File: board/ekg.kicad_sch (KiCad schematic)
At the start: 48 parts

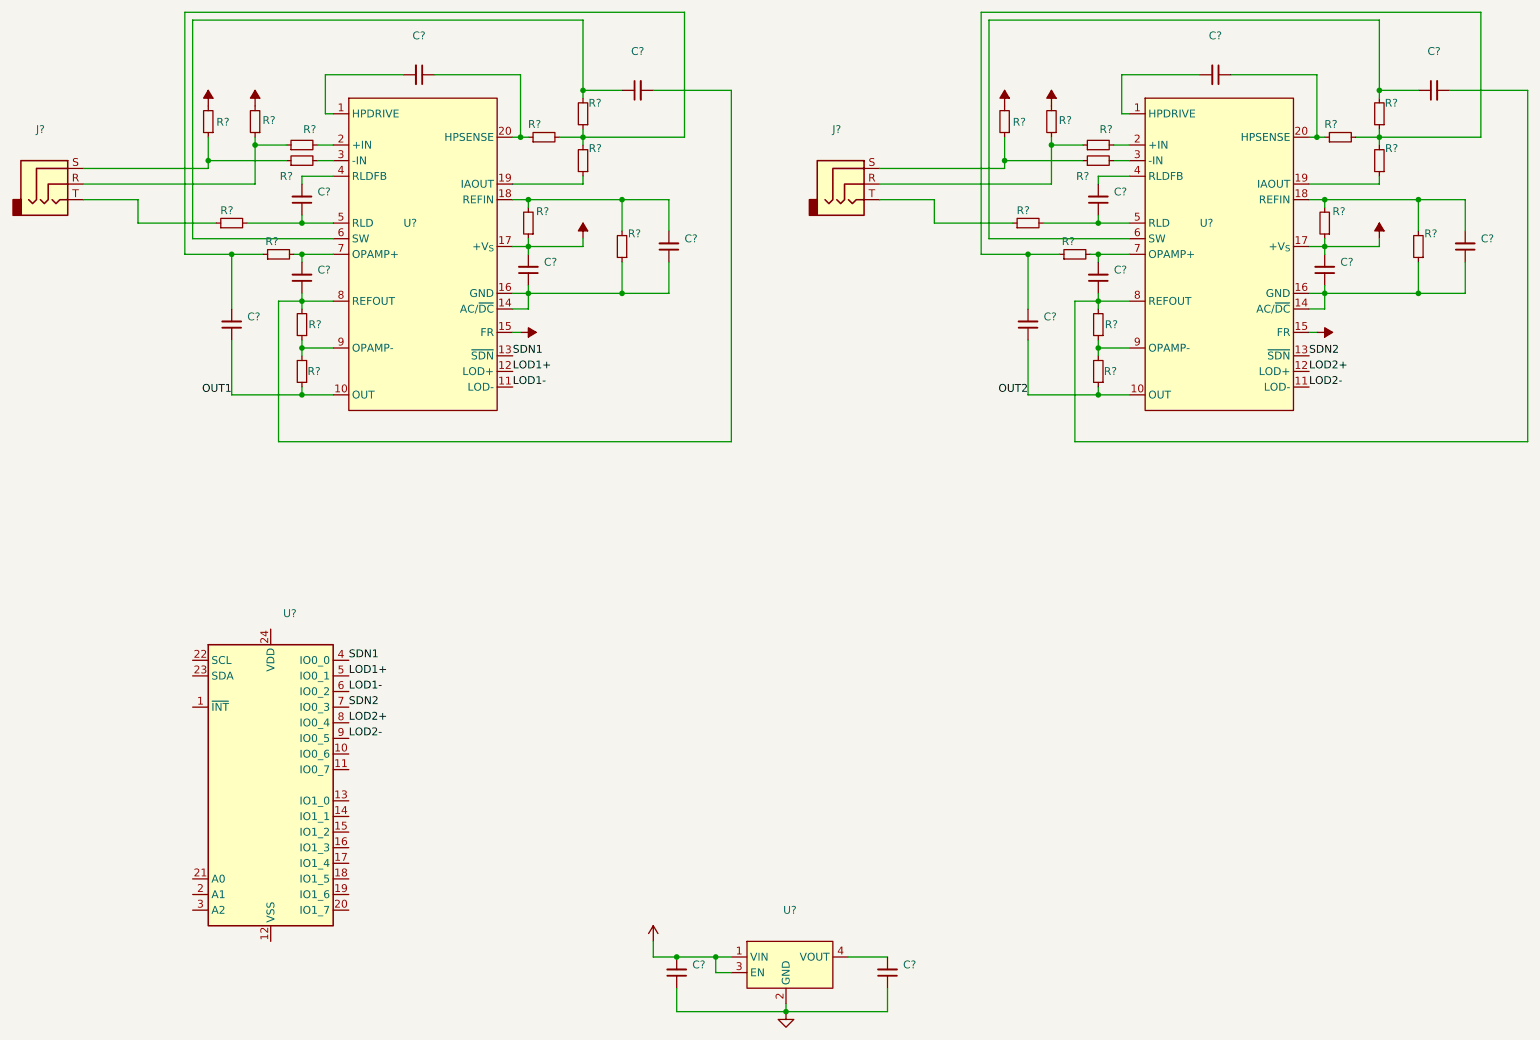
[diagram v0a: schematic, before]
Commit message: added ekg chip
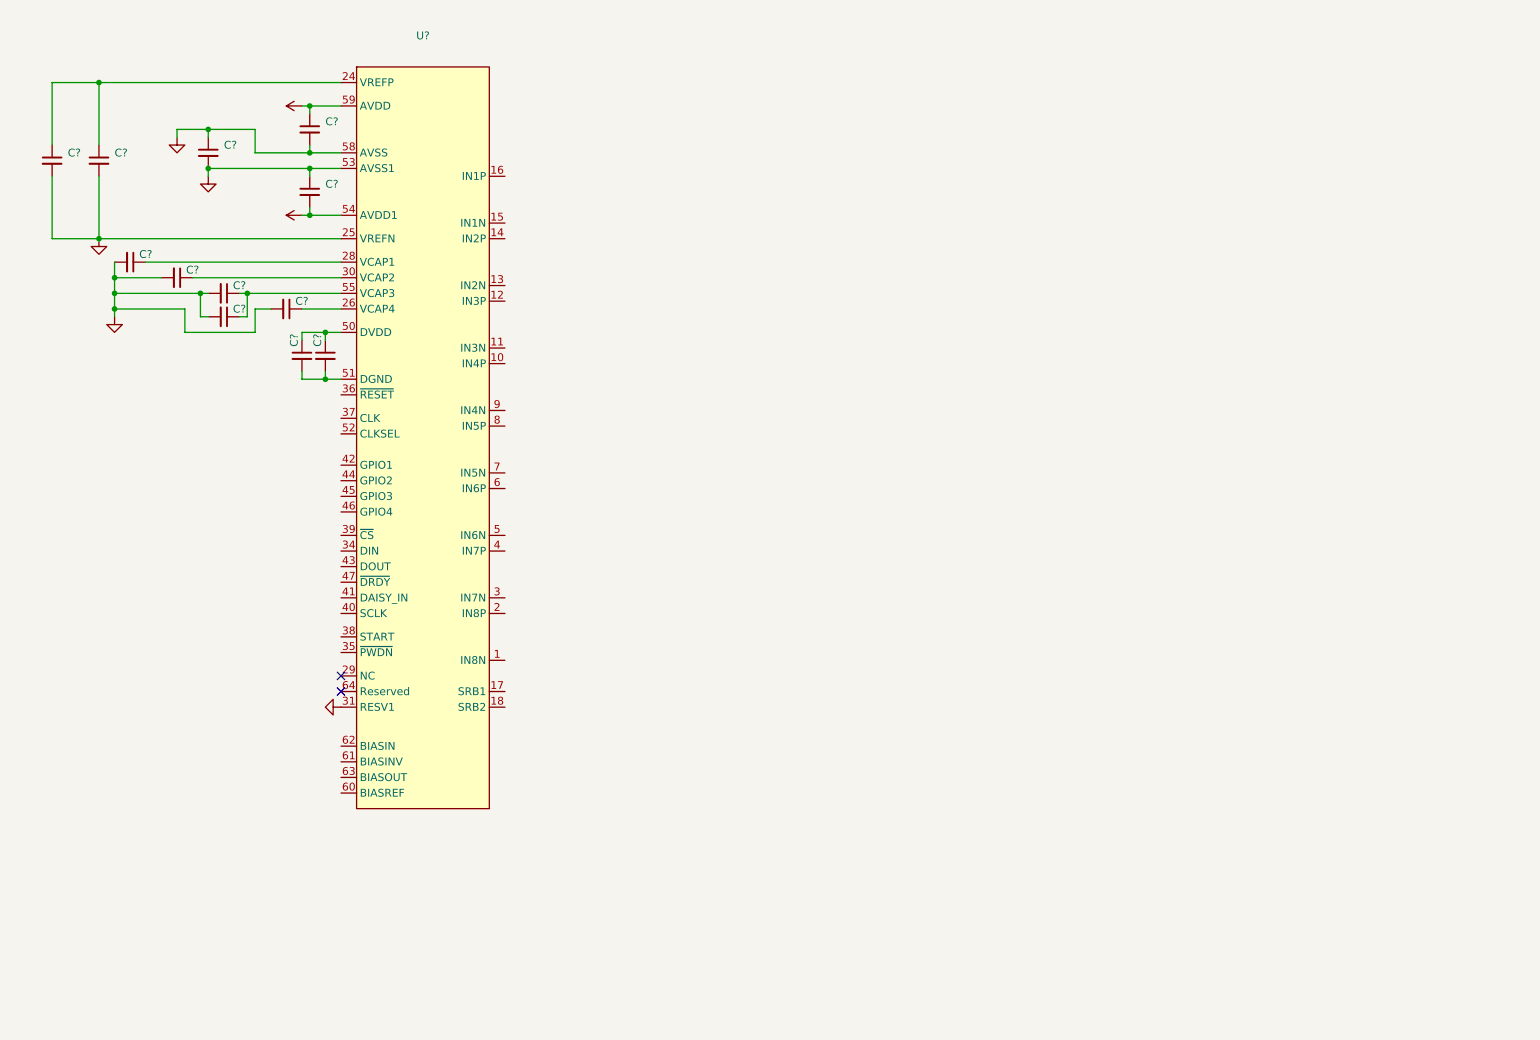
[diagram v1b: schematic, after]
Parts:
- removed C? (x9): (no value), symbol Device:C_Small
- removed C? (x7): ~, symbol Device:C_Small
- removed J? (x2): ~, symbol Connector:AudioJack3
- removed R? (x17): (no value), symbol Device:R_Small
- removed R? (x9): ~, symbol Device:R_Small
- removed U? (x2): ~, symbol ownLib:AD8232
- removed U?: (no value), symbol ownLib:ADP150
- removed U?: (no value), symbol Interface_Expansion:PCA9555D
- added C? (x11): (no value), symbol Device:C_Small
- added C?: ~, symbol Device:C_Small
- added U?: (no value), symbol ownLib:ADS1299-x
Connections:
- new net: C?.1, U?.26 (VCAP4)
- new net: C?.1, C?.1, U?.24 (VREFP)
- new net: U?.27 (NC), U?.29 (NC)
- new net: C?.1, U?.28 (VCAP1)
- new net: C?.1, U?.30 (VCAP2)
- new net: C?.1, C?.1, U?.55 (VCAP3)
- new net AVDD: C?.1, C?.2, U?.19 (AVDD), U?.21 (AVDD), U?.22 (AVDD), U?.54 (AVDD1), U?.56 (AVDD), U?.59 (AVDD)
- new net AVSS: C?.1, C?.1, C?.2, C?.2, C?.2, C?.2, C?.2, C?.2, C?.2, C?.2, C?.2, U?.20 (AVSS), U?.23 (AVSS), U?.25 (VREFN), U?.31 (RESV1), U?.32 (AVSS), U?.53 (AVSS1), U?.57 (AVSS), U?.58 (AVSS)
- new net DGND: C?.2, C?.2, U?.33 (DGND), U?.49 (DGND), U?.51 (DGND)
- new net DVDD: C?.1, C?.1, U?.48 (DVDD), U?.50 (DVDD)
- no-connect marks 0 -> 2

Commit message: added filter and imu
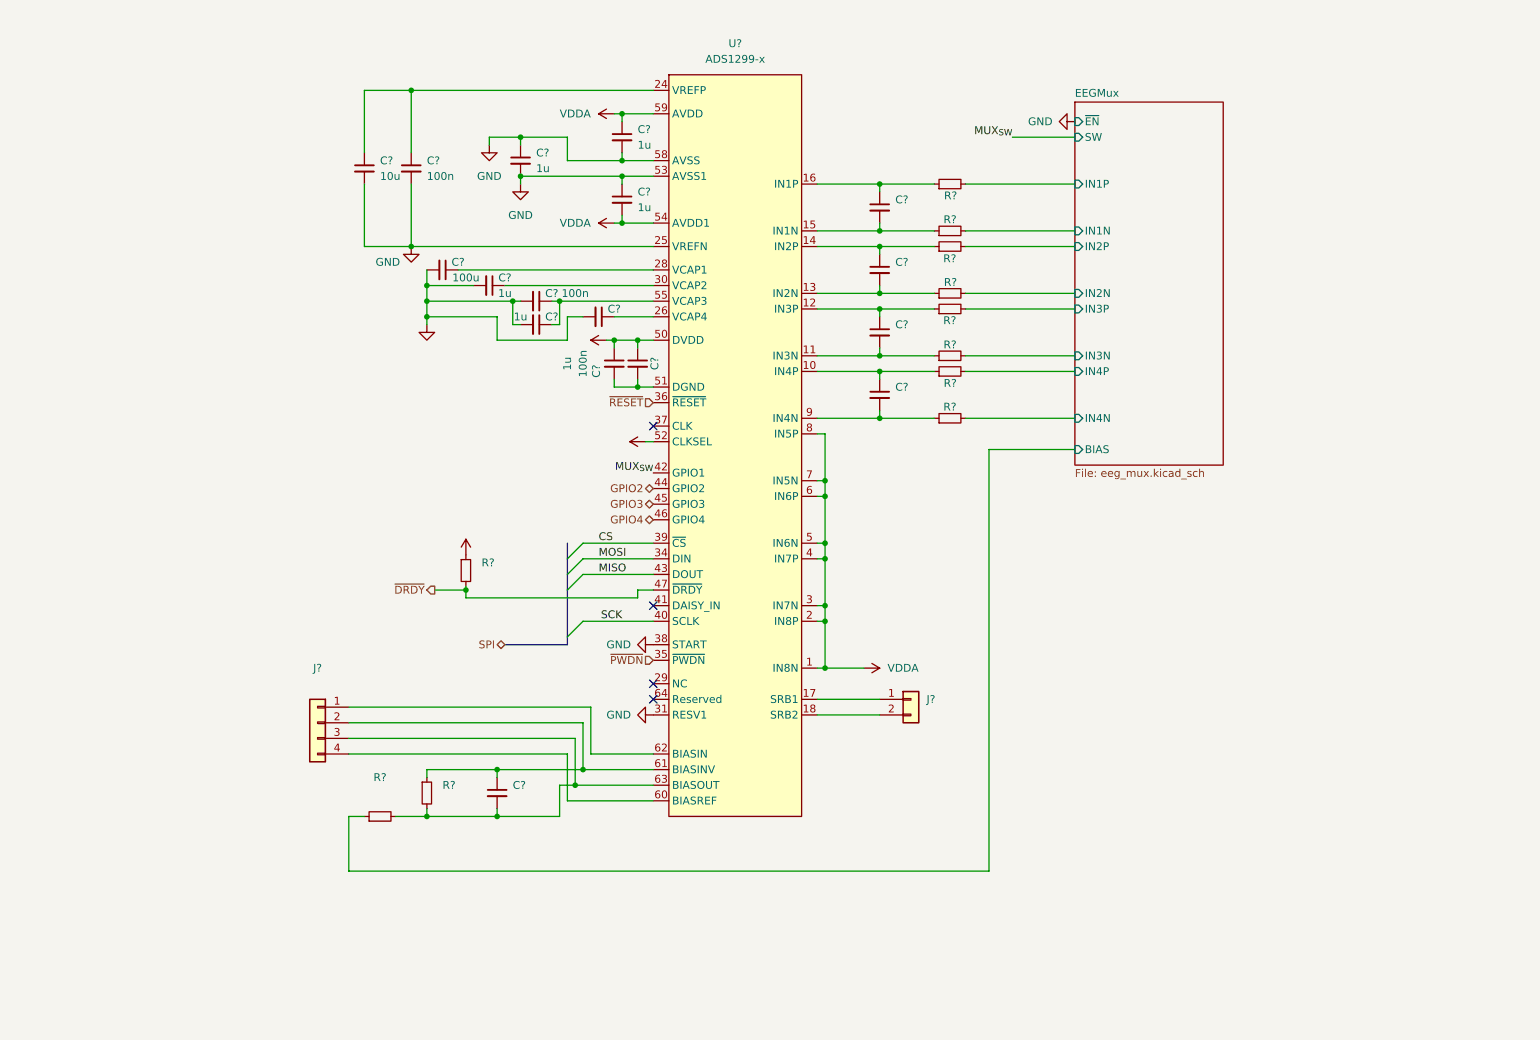
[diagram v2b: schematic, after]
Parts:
- added C? (x5): (no value), symbol Device:C_Small
- added J?: (no value), symbol Connector_Generic:Conn_01x02
- added J?: (no value), symbol Connector_Generic:Conn_01x04
- added R? (x10): (no value), symbol Device:R_Small
- added R?: ~, symbol Device:R_Small
- C? (x6): value (none) -> 1u
- C? (x3): value (none) -> 100n
- C?: value (none) -> 100u
- C?: value (none) -> 10u
- U?: value (none) -> ADS1299-x
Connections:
- net AVDD: now also U?.1 (IN8N), U?.2 (IN8P), U?.3 (IN7N), U?.4 (IN7P), U?.5 (IN6N), U?.6 (IN6P), U?.7 (IN5N), U?.8 (IN5P)
- net AVSS: now also U?.38 (START)
- net DVDD: now also U?.52 (CLKSEL), R?.1
- net at U?.10 (IN4P): now also C?.1, R?.1
- net at U?.11 (IN3N): now also C?.2, R?.1
- net at U?.12 (IN3P): now also C?.1, R?.1
- net at U?.13 (IN2N): now also C?.2, R?.1
- net at U?.14 (IN2P): now also C?.1, R?.1
- net at U?.15 (IN1N): now also C?.2, R?.1
- net at U?.16 (IN1P): now also C?.1, R?.1
- net at U?.17 (SRB1): now also J?.1 (Pin_1)
- net at U?.18 (SRB2): now also J?.2 (Pin_2)
- net MOSI: now reaches U?.34 (DIN)
- net ~{PWDN}: now reaches U?.35 (~{PWDN})
- net ~{RESET}: now reaches U?.36 (~{RESET})
- net CS: now reaches U?.39 (~{CS})
- net SCK: now reaches U?.40 (SCLK)
- net MUX_{SW}: now reaches U?.42 (GPIO1)
- net MISO: now reaches U?.43 (DOUT)
- net GPIO2: now reaches U?.44 (GPIO2)
- net GPIO3: now reaches U?.45 (GPIO3)
- net GPIO4: now reaches U?.46 (GPIO4)
- net ~{DRDY}: now reaches U?.47 (~{DRDY})
- net ~{DRDY}: now also R?.2
- net at U?.60 (BIASREF): now also J?.4 (Pin_4)
- net at U?.61 (BIASINV): now also C?.1, J?.2 (Pin_2), R?.1
- net at U?.62 (BIASIN): now also J?.1 (Pin_1)
- net at U?.63 (BIASOUT): now also C?.2, J?.3 (Pin_3), R?.2, R?.2
- net at U?.9 (IN4N): now also C?.2, R?.1
- new net EEGMux/BIAS: R?.1
- new net EEGMux/IN1N: R?.2
- new net EEGMux/IN1P: R?.2
- new net EEGMux/IN2N: R?.2
- new net EEGMux/IN2P: R?.2
- new net EEGMux/IN3N: R?.2
- new net EEGMux/IN3P: R?.2
- new net EEGMux/IN4N: R?.2
- new net EEGMux/IN4P: R?.2
- no-connect marks 2 -> 4
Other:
- added sheet EEGMux (eeg_mux.kicad_sch)
- moved on the sheet: C?, U?

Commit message: updated hw project
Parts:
- C? (x4): value (none) -> C_{Filt}
- C?: value (none) -> C_{F}
- J?: value (none) -> SRB
- J?: value (none) -> BIAS
- R? (x8): value (none) -> R_{Filt}
- R?: value (none) -> R_{P}
- R?: value (none) -> R_{F}
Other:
- note added: "TODO: Jumper"
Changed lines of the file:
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@@
     (stroke (width 0) (type default) (color 0 0 0 0))
+  )
+  (text "TODO: Jumper" (at 109.22 156.21 0)
+    (effects (font (size 1.27 1.27)) (justify left bottom))
   )
   (label "MOSI" (at 113.03 113.03 0)
@@
     (in_bom yes) (on_board yes)
     (property "Reference" "R?" (id 0) (at 170.174 88.324 90))
-    (property "Value" "" (id 1) (at 170.18 90.17 90))
+    (property "Value" "R_{Filt}" (id 1) (at 170.18 90.17 90))
     (property "Footprint" "" (id 2) (at 170.18 90.17 0)
       (effects (font (size 1.27 1.27)) hide)
@@
     (in_bom yes) (on_board yes) (fields_autoplaced)
     (property "Reference" "R?" (id 0) (at 77.47 148.59 90))
-    (property "Value" "" (id 1) (at 77.47 151.13 90))
+    (property "Value" "R_{P}" (id 1) (at 77.47 151.13 90))
     (property "Footprint" "" (id 2) (at 77.47 154.94 0)
       (effects (font (size 1.27 1.27)) hide)
@@
       (effects (font (size 1.27 1.27)) (justify left))
     )
-    (property "Value" "" (id 1) (at 161.29 87.6362 0)
+    (property "Value" "C_{Filt}" (id 1) (at 161.29 87.6362 0)
       (effects (font (size 1.27 1.27)) (justify left))
     )
@@
     (in_bom yes) (on_board yes)
     (property "Reference" "R?" (id 0) (at 170.2658 68.0484 90))
-    (property "Value" "" (id 1) (at 170.18 69.85 90))
+    (property "Value" "R_{Filt}" (id 1) (at 170.18 69.85 90))
     (property "Footprint" "" (id 2) (at 170.18 69.85 0)
       (effects (font (size 1.27 1.27)) hide)
@@
     (in_bom yes) (on_board yes)
     (property "Reference" "R?" (id 0) (at 170.2887 53.9655 90))
-    (property "Value" "" (id 1) (at 170.18 52.07 90))
+    (property "Value" "R_{Filt}" (id 1) (at 170.18 52.07 90))
     (property "Footprint" "" (id 2) (at 170.18 52.07 0)
       (effects (font (size 1.27 1.27)) hide)
@@
     (in_bom yes) (on_board yes)
     (property "Reference" "R?" (id 0) (at 170.197 57.8418 90))
-    (property "Value" "" (id 1) (at 170.18 59.69 90))
+    (property "Value" "R_{Filt}" (id 1) (at 170.18 59.69 90))
     (property "Footprint" "" (id 2) (at 170.18 59.69 0)
       (effects (font (size 1.27 1.27)) hide)
@@
       (effects (font (size 1.27 1.27)) (justify left))
     )
-    (property "Value" "" (id 1) (at 166.37 138.4299 0)
+    (property "Value" "SRB" (id 1) (at 166.37 138.4299 0)
       (effects (font (size 1.27 1.27)) (justify left))
     )
@@
       (effects (font (size 1.27 1.27)) hide)
     )
-    (property "Value" "" (id 1) (at 112.2845 76.2722 90)
+    (property "Value" "VDD" (id 1) (at 112.2845 76.2722 90)
       (effects (font (size 1.27 1.27)) (justify left))
     )
@@
     (in_bom yes) (on_board yes)
     (property "Reference" "R?" (id 0) (at 170.2199 84.4707 90))
-    (property "Value" "" (id 1) (at 170.18 82.55 90))
+    (property "Value" "R_{Filt}" (id 1) (at 170.18 82.55 90))
     (property "Footprint" "" (id 2) (at 170.18 82.55 0)
       (effects (font (size 1.27 1.27)) hide)
@@
     (in_bom yes) (on_board yes) (fields_autoplaced)
     (property "Reference" "J?" (id 0) (at 67.31 130.81 0))
-    (property "Value" "" (id 1) (at 67.31 133.35 0))
+    (property "Value" "BIAS" (id 1) (at 67.31 133.35 0))
     (property "Footprint" "" (id 2) (at 67.31 139.7 0)
       (effects (font (size 1.27 1.27)) hide)
@@
     (in_bom yes) (on_board yes)
     (property "Reference" "R?" (id 0) (at 170.197 78.2091 90))
-    (property "Value" "" (id 1) (at 170.18 80.01 90))
+    (property "Value" "R_{Filt}" (id 1) (at 170.18 80.01 90))
     (property "Footprint" "" (id 2) (at 170.18 80.01 0)
       (effects (font (size 1.27 1.27)) hide)
@@
       (effects (font (size 1.27 1.27)) (justify left))
     )
-    (property "Value" "" (id 1) (at 161.29 57.1562 0)
+    (property "Value" "C_{Filt}" (id 1) (at 161.29 57.1562 0)
       (effects (font (size 1.27 1.27)) (justify left))
     )
@@
       (effects (font (size 1.27 1.27)) (justify left))
     )
-    (property "Value" "" (id 1) (at 99.06 152.4062 0)
+    (property "Value" "C_{F}" (id 1) (at 99.06 152.4062 0)
       (effects (font (size 1.27 1.27)) (justify left))
     )
@@
       (effects (font (size 1.27 1.27)) hide)
     )
-    (property "Value" "" (id 1) (at 118.6345 92.7822 90)
+    (property "Value" "VDD" (id 1) (at 118.6345 92.7822 90)
       (effects (font (size 1.27 1.27)) (justify left))
     )
@@
       (effects (font (size 1.27 1.27)) (justify left))
     )
-    (property "Value" "" (id 1) (at 161.29 67.3162 0)
+    (property "Value" "C_{Filt}" (id 1) (at 161.29 67.3162 0)
       (effects (font (size 1.27 1.27)) (justify left))
     )
@@
       (effects (font (size 1.27 1.27)) (justify left))
     )
-    (property "Value" "" (id 1) (at 87.63 152.3999 0)
+    (property "Value" "R_{F}" (id 1) (at 87.63 152.3999 0)
       (effects (font (size 1.27 1.27)) (justify left))
     )
@@
       (effects (font (size 1.27 1.27)) hide)
     )
-    (property "Value" "" (id 1) (at 92.6378 110.3795 90)
+    (property "Value" "VDD" (id 1) (at 92.6378 110.3795 90)
       (effects (font (size 1.27 1.27)) (justify left))
     )
@@
       (effects (font (size 1.27 1.27)) (justify left))
     )
-    (property "Value" "" (id 1) (at 161.29 77.4762 0)
+    (property "Value" "C_{Filt}" (id 1) (at 161.29 77.4762 0)
       (effects (font (size 1.27 1.27)) (justify left))
     )
@@
     (in_bom yes) (on_board yes)
     (property "Reference" "R?" (id 0) (at 170.1511 74.2641 90))
-    (property "Value" "" (id 1) (at 170.18 72.39 90))
+    (property "Value" "R_{Filt}" (id 1) (at 170.18 72.39 90))
     (property "Footprint" "" (id 2) (at 170.18 72.39 0)
       (effects (font (size 1.27 1.27)) hide)
@@
     (in_bom yes) (on_board yes)
     (property "Reference" "R?" (id 0) (at 170.1511 64.1951 90))
-    (property "Value" "" (id 1) (at 170.18 62.23 90))
+    (property "Value" "R_{Filt}" (id 1) (at 170.18 62.23 90))
     (property "Footprint" "" (id 2) (at 170.18 62.23 0)
       (effects (font (size 1.27 1.27)) hide)

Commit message: updated schematic
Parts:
- added JP? (x2): BIASOUT SEL, symbol Jumper:Jumper_3_Bridged12
- added JP?: BIASINV SEL, symbol Jumper:Jumper_3_Bridged12
- J?: symbol Connector_Generic:Conn_01x04 -> Connector_Generic:Conn_01x05
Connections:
- net DVDD: no longer R?.1, U?.52 (CLKSEL)
- net EEGMux/BIAS: now also JP?.2 (C); no longer R?.1
- net at C?.2, R?.2, R?.2: now also JP?.1 (A); no longer J?.3 (Pin_3), U?.63 (BIASOUT)
- net at C?.1, R?.1: now also JP?.1 (A); no longer J?.2 (Pin_2), U?.61 (BIASINV)
- net AVDD renamed +5VA
- net +5VA: no longer C?.1, U?.19 (AVDD), U?.21 (AVDD), U?.22 (AVDD), U?.56 (AVDD), U?.59 (AVDD)
- new net: JP?.1 (A), R?.1
- new net: J?.5 (Pin_5), JP?.3 (B)
- new net: JP?.2 (C), U?.61 (BIASINV)
- new net: JP?.2 (C), U?.63 (BIASOUT)
- new net: J?.3 (Pin_3), JP?.3 (B)
- new net: J?.2 (Pin_2), JP?.3 (B)
- new net +3V3: C?.1, U?.19 (AVDD), U?.21 (AVDD), U?.22 (AVDD), U?.52 (CLKSEL), U?.56 (AVDD), U?.59 (AVDD)
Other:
- sheet EEGMux ports: added none; removed SW, ~{EN}
- note added: "Jumper to include Filter"
- note removed: "TODO: Jumper"
- moved on the sheet: C?, R?
